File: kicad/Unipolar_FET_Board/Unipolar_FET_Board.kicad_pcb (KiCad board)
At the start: 2 copper layers, 200 x 127 mm, 18 parts, among them J1 Screw_Terminal_01x04, J3 SENSE, J4 N-MOS, Q1 Q_NMOS_GDS, Q2 Q_NMOS_GDS

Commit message: Added vias'
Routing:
- net Load_cold: vias 0 -> 4
- net GND: vias 15 -> 16
- net +HCC: vias 0 -> 4
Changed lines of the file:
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@@
+	)
+	(via
+		(at 194.564 106.68)
+		(size 2)
+		(drill 1)
+		(layers "F.Cu" "B.Cu")
+		(free yes)
+		(net 1)
 	)
 	(via
@@
 		(width 1)
 		(layer "F.Cu")
+		(net 2)
+	)
+	(via
+		(at 181.864 67.564)
+		(size 2)
+		(drill 1)
+		(layers "F.Cu" "B.Cu")
+		(free yes)
+		(net 2)
+	)
+	(via
+		(at 181.864 80.772)
+		(size 2)
+		(drill 1)
+		(layers "F.Cu" "B.Cu")
+		(free yes)
+		(net 2)
+	)
+	(via
+		(at 201.676 84.836)
+		(size 2)
+		(drill 1)
+		(layers "F.Cu" "B.Cu")
+		(free yes)
+		(net 2)
+	)
+	(via
+		(at 208.28 64.008)
+		(size 2)
+		(drill 1)
+		(layers "F.Cu" "B.Cu")
+		(free yes)
 		(net 2)
 	)
@@
 		(net 9)
 	)
+	(via
+		(at 183.388 89.408)
+		(size 2)
+		(drill 1)
+		(layers "F.Cu" "B.Cu")
+		(free yes)
+		(net 10)
+	)
+	(via
+		(at 183.388 93.472)
+		(size 2)
+		(drill 1)
+		(layers "F.Cu" "B.Cu")
+		(free yes)
+		(net 10)
+	)
+	(via
+		(at 183.388 101.092)
+		(size 2)
+		(drill 1)
+		(layers "F.Cu" "B.Cu")
+		(free yes)
+		(net 10)
+	)
+	(via
+		(at 183.388 97.536)
+		(size 2)
+		(drill 1)
+		(layers "F.Cu" "B.Cu")
+		(free yes)
+		(net 10)
+	)
 	(zone

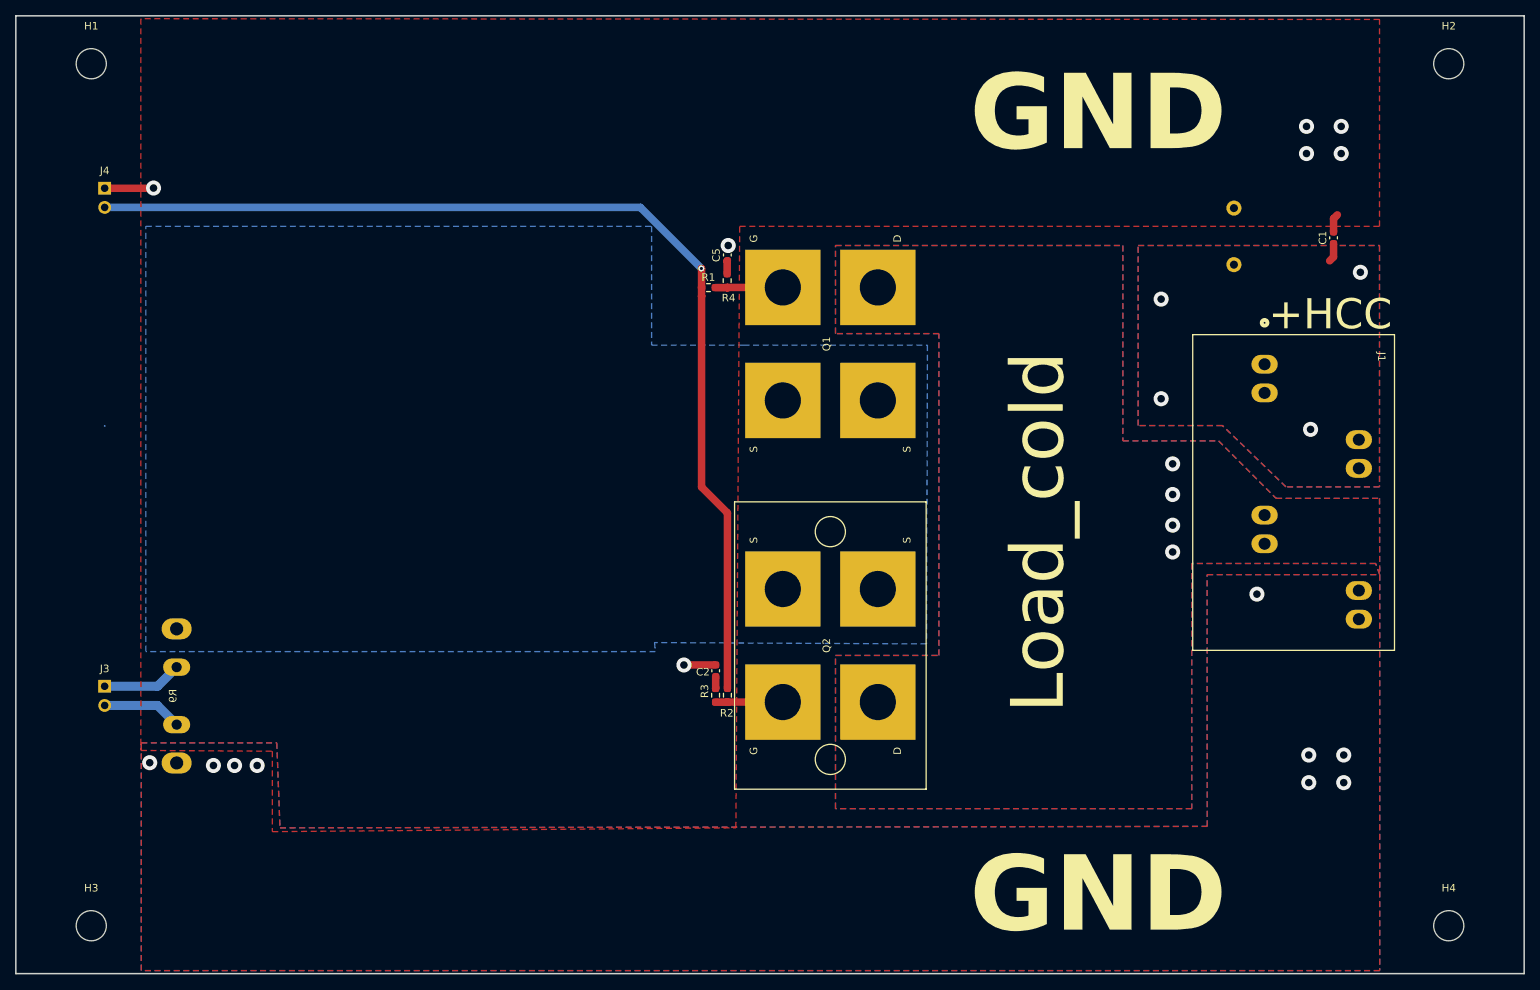
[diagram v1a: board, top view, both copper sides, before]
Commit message: Added varistor and labesl for the connecters
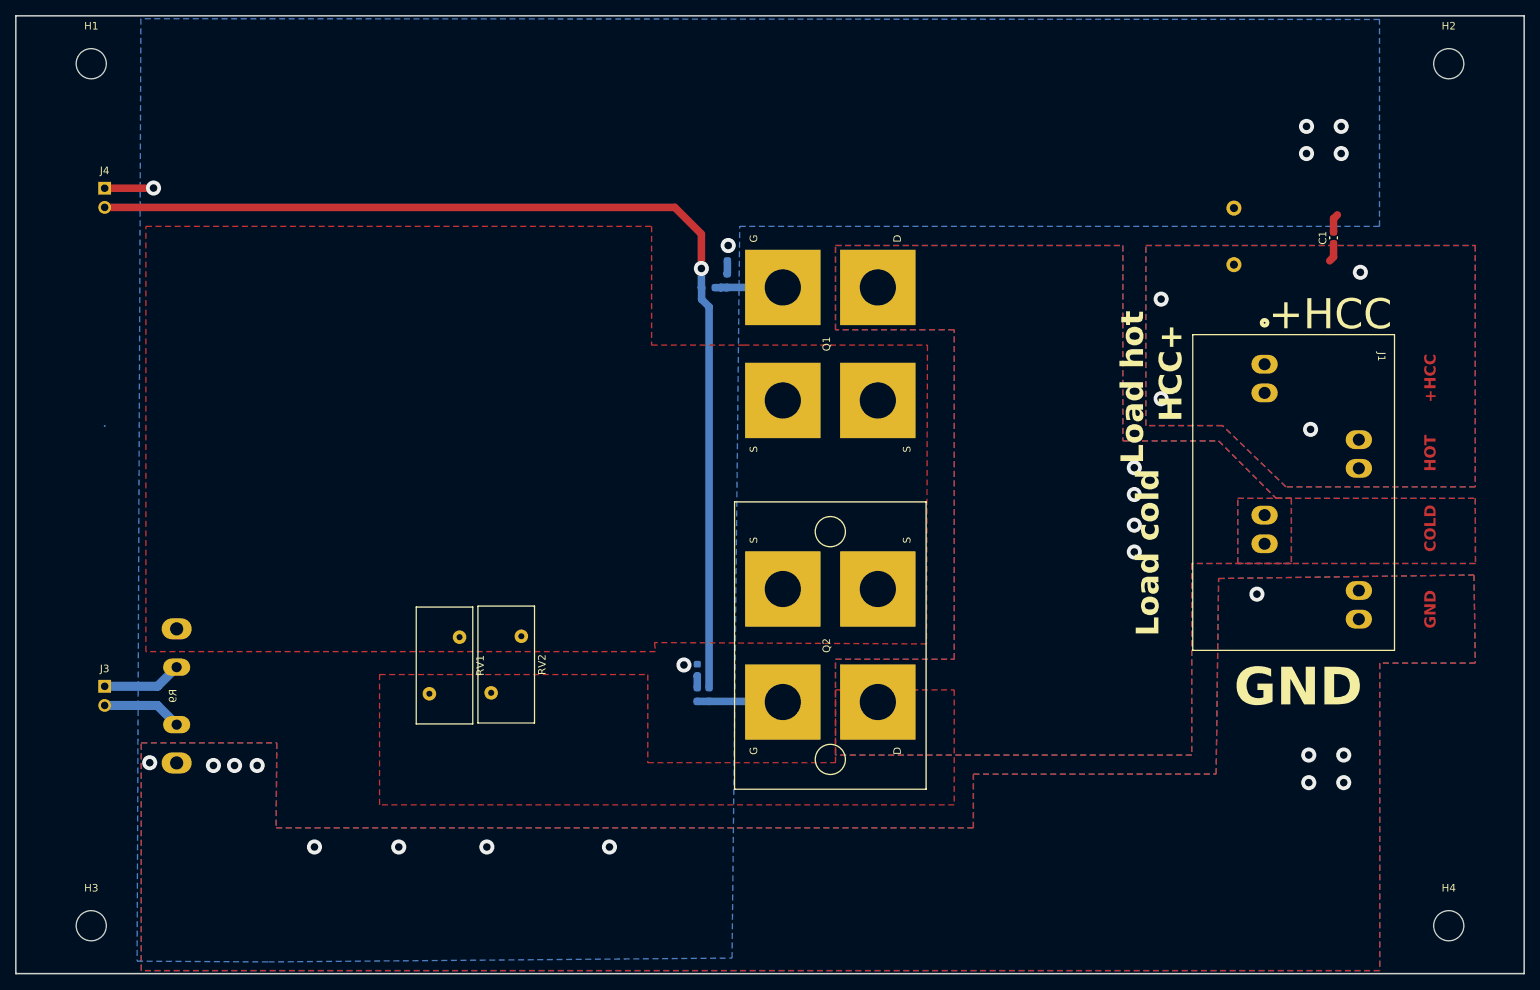
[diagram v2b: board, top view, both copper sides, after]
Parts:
- added RV1: V20E50P (80V), Varistor:RV_Disc_D15.5mm_W7.5mm_P7.5mm, F.Cu at (84.8, 119.9)
- added RV2: V20E50P (80V), Varistor:RV_Disc_D15.5mm_W7.5mm_P7.5mm, F.Cu at (93.0, 119.8)
- C2, C5, R1, R2, R3, R4: moved to B.Cu
- moved R2 2.44 mm to (121.9, 120.0)
- moved R3 2.44 mm to (120.4, 120.0)
- moved C2 2.44 mm to (120.4, 116.7)
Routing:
- net GND: track 13.2 -> 8.99 mm, vias 16 -> 20
- net Net-(Q2-G): track 8.93 -> 11.4 mm
- net Net-(J4-Pin_2): track 139.6 -> 141.2 mm
- net Net-(Q1-G): track 9.02 -> 9.86 mm
- added copper zone on F.Cu, net Net-(Q1-S)
- removed copper zone on B.Cu, net Net-(Q1-S)
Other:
- board text added: "COLD"
- board text added: "HCC+"
- board text added: "HOT"
- board text added: "Load cold"
- board text added: "Load hot"
- board text removed: "Load_cold"
- board text removed: "MOS_SOURCE"

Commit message: Parallel MOS with current sharing resistors
Putting additional resistors in series with the source of each MOS is not necessary.
Nonetheless I saved this partiular snapshot in case we want to pursuit this strategy to share the current
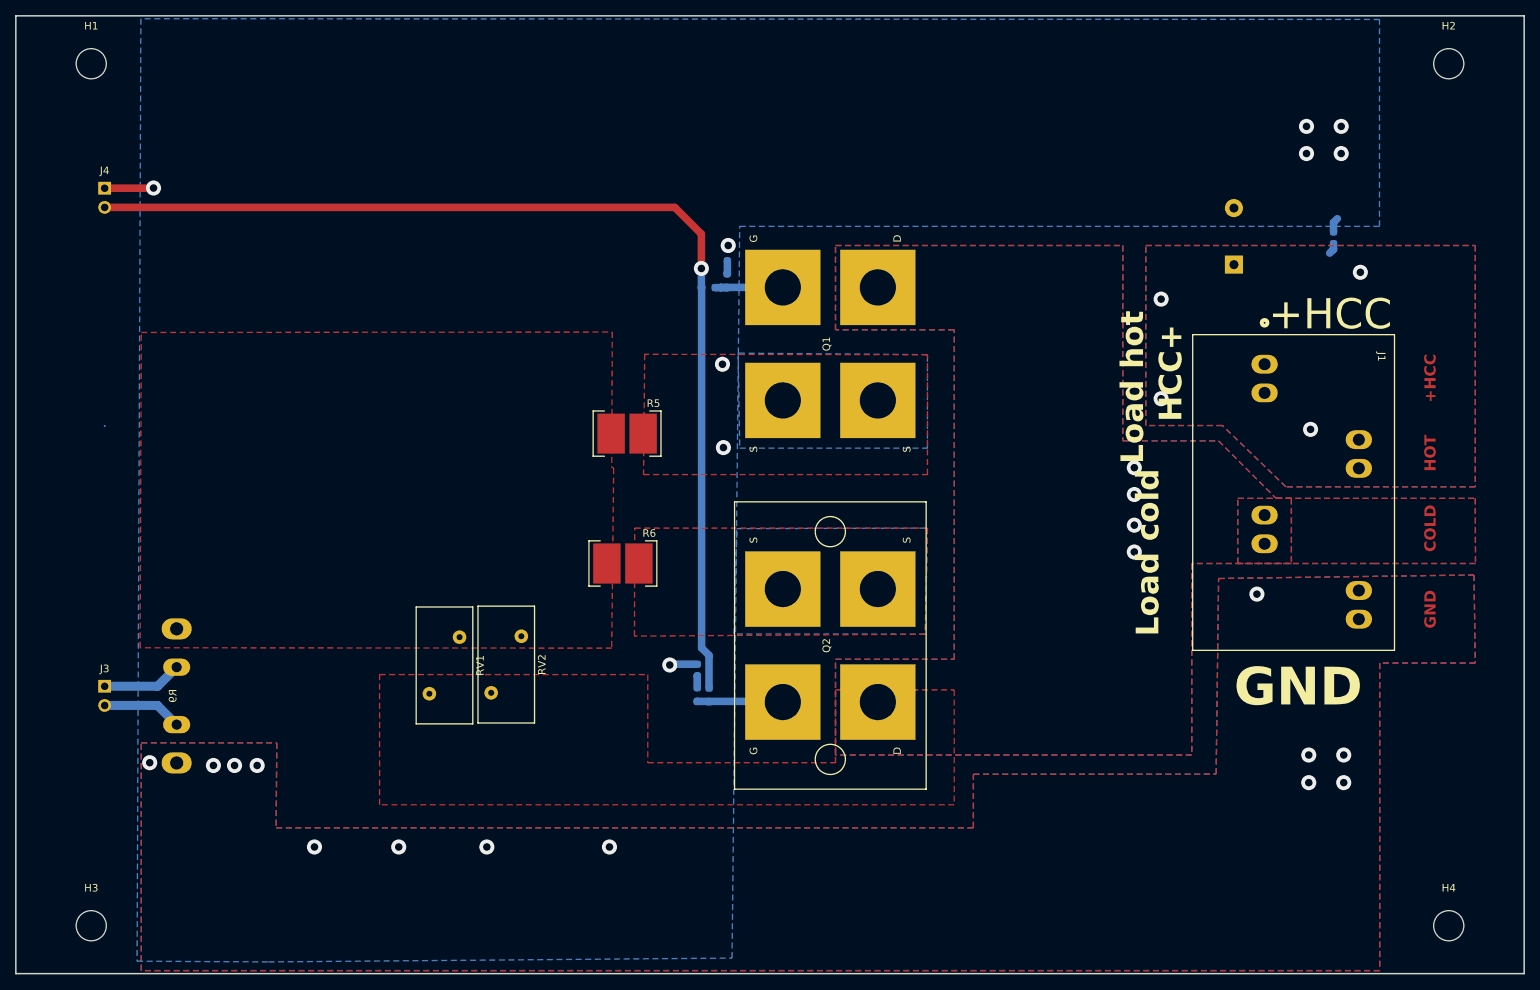
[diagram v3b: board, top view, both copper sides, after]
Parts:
- added R5: 20, zmyfootprint:res_2818, F.Cu at (111.0, 85.4)
- added R6: 20, zmyfootprint:res_2818, F.Cu at (110.5, 102.6)
- C1: moved to B.Cu
- C3: footprint Capacitor_THT:CAP_UBY_18X35P5_NCH -> Capacitor_THT:CP_Radial_D18.0mm_P7.50mm
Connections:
- Q2 pad 3: Net-(Q1-S) -> Net-(Q2-S)
- R9 pad 1: Net-(Q1-S) -> /RETURN
- RV1 pad 2: Net-(Q1-S) -> /RETURN
- RV2 pad 2: Net-(Q1-S) -> /RETURN
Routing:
- net GND: track 8.99 -> 12.2 mm
- net +HCC: track 2.55 -> 1.53 mm
- net Net-(Q1-S): vias 0 -> 2
- added copper zone on F.Cu, net /RETURN
- added copper zone on B.Cu, net Net-(Q1-S)
- added copper zone on B.Cu, net Net-(Q2-S)
- added copper zone on F.Cu, net Net-(Q2-S)
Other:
- rule pad_to_mask_clearance: 0.2 -> 0.15

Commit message: The MOS and capacitors are now in the correct orientation
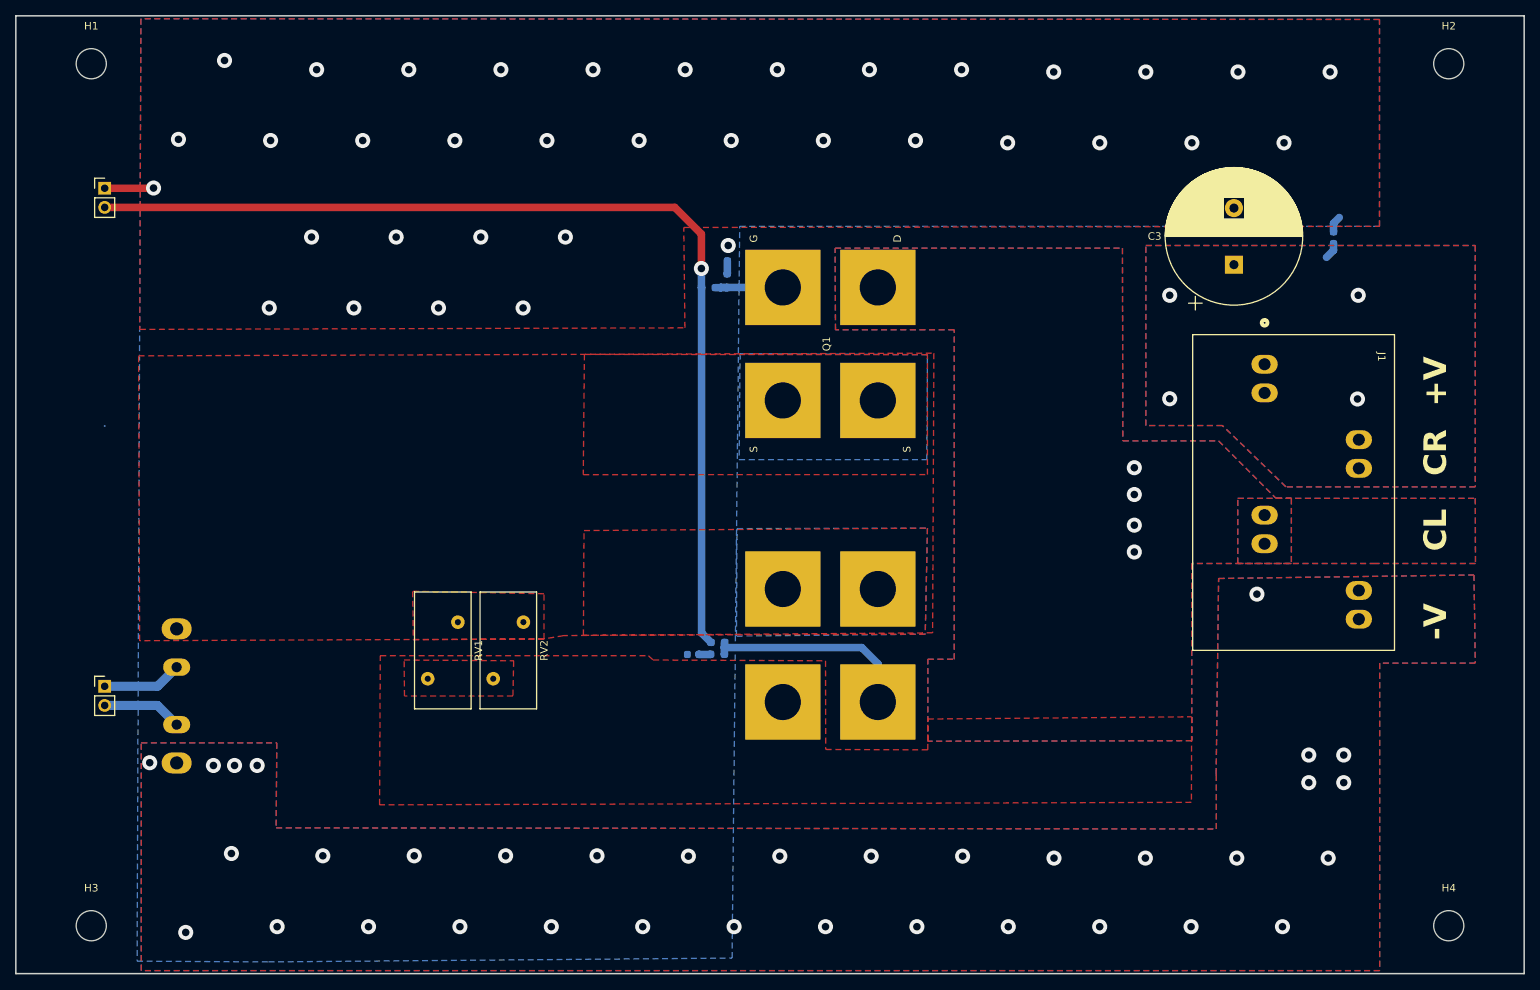
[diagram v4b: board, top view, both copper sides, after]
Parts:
- removed R5, R6: 20, zmyfootprint:res_2818
- C3, J3, J4, R9: moved to F.Cu
- Q2: moved to B.Cu
- moved R2 7.06 mm to (123.1, 113.1), turned to 180 degrees
- moved R3 5.98 mm to (123.0, 114.6), turned to 180 degrees
- moved C2 2.14 mm to (119.8, 114.7), turned to 0 degrees
- moved RV1 2.00 mm to (84.6, 117.9)
- moved RV2 1.89 mm to (93.3, 117.9)
- turned J3 to 0 degrees
- turned J4 to 0 degrees
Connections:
- Q1 pad 3: Net-(Q1-S) -> /RETURN
- Q2 pad 3: Net-(Q2-S) -> /RETURN
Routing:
- net Net-(Q2-G): track 11.4 -> 27.9 mm
- net Net-(J4-Pin_2): track 141.2 -> 135.3 mm
- net GND: track 12.2 -> 8.71 mm, vias 20 -> 71
- net +HCC: track 1.53 -> 2.28 mm
- net Net-(Q1-S): vias 2 -> 0
- added copper zone on B.Cu, net /RETURN
- removed copper zone on B.Cu, net Net-(Q1-S)
- removed copper zone on F.Cu, net Net-(Q1-S)
- removed copper zone on B.Cu, net Net-(Q2-S)
- removed copper zone on F.Cu, net Net-(Q2-S)
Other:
- rule pad_to_mask_clearance: 0.15 -> 0
- board text added: "+V"
- board text added: "-V"
- board text added: "CL"
- board text added: "CR"
- board text removed: "+HCC"
- board text removed: "COLD"
- board text removed: "GND"
- board text removed: "HCC+"
- board text removed: "HOT"
- board text removed: "Load cold"
- board text removed: "Load hot"
